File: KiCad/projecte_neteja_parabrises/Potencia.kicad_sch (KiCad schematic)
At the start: 18 parts, among them K1 DIPxx-1Axx-12xD, K2 G6K-2, Q1 NPN

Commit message: SCH V1
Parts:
- HEATER: value R -> 1K
- R: renamed from R1; value R -> 4.7K
- R1: renamed from 1k; value R -> 4.7K
- R2, R3: value 10K -> 1k
- gave numbers to parts that had none: 8
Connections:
- net VDD is gone; now on net 12V: D1.1 (K), K1.13, K1.2, K1.7, K1.8, K2.1, K2.3, K2.6
- net GND: now also U2.2 (IN2), U3.2 (IN2)
- net micro: no longer R1.1
- net GATE C: now reaches R.1
- net PWM: now reaches U2.3 (IN1)
- net PWM: now also U3.3 (IN1)
- net 12V: now reaches U2.5 (VM)
- net 12V: now also U3.5 (VM)
- new net GATE B: R1.1
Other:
- note added: "BOMBAS Y CIRCUITO RELE"
- note added: "CIRCUITO RELE Y CALEFACTOR"
- note added: "DRIVERS Y MOTORES"
- note added: "FINAL DE CARRERA"
- moved on the sheet: D1, FINALCARRERA1, FINALCARRERA2, HEATER, K1, K2, M1, M2, M3, M4, Q1, R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

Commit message: UART ACABADO
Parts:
- renumbered FINALCARRERA2 to FINALCARRERA1, FINALCARRERA1 to FINALCARRERA2, HEATER to HEATER1, K2 to K1, K1 to K2, Q1 to Q2, R to R4
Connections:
- no-connect marks 2 -> 6
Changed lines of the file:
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@@
+	)
+	(no_connect
+		(at 21.59 20.32)
+	)
+	(no_connect
+		(at 41.275 34.925)
+	)
+	(no_connect
+		(at -13.97 45.72)
+	)
+	(no_connect
+		(at 41.275 65.405)
 	)
 	(no_connect
@@
 		(on_board yes)
 		(dnp no)
-		(property "Reference" "#PWR?"
+		(property "Reference" "#PWR014"
 			(at 31.115 46.355 0)
 			(effects
@@
 			(project "projecte_neteja_parabrises"
 				(path "/83fe8808-b70b-463e-9fcd-89556c9690a9/54835b05-573d-4299-97f2-a5366b1fd616"
-					(reference "#PWR?")
+					(reference "#PWR014")
 					(unit 1)
 				)
@@
 		(dnp no)
 		(fields_autoplaced yes)
-		(property "Reference" "FINALCARRERA?"
+		(property "Reference" "FINALCARRERA2"
 			(at 45.085 99.695 0)
 			(effects
@@
 			(project "projecte_neteja_parabrises"
 				(path "/83fe8808-b70b-463e-9fcd-89556c9690a9/54835b05-573d-4299-97f2-a5366b1fd616"
-					(reference "FINALCARRERA?")
+					(reference "FINALCARRERA2")
 					(unit 1)
 				)
@@
 		(dnp no)
 		(fields_autoplaced yes)
-		(property "Reference" "#PWR?"
+		(property "Reference" "#PWR021"
 			(at 254 27.305 0)
 			(effects
@@
 			(project "projecte_neteja_parabrises"
 				(path "/83fe8808-b70b-463e-9fcd-89556c9690a9/54835b05-573d-4299-97f2-a5366b1fd616"
-					(reference "#PWR?")
+					(reference "#PWR021")
 					(unit 1)
 				)
@@
 		(dnp no)
 		(fields_autoplaced yes)
-		(property "Reference" "#PWR?"
+		(property "Reference" "#PWR016"
 			(at 33.655 92.71 0)
 			(effects
@@
 			(project "projecte_neteja_parabrises"
 				(path "/83fe8808-b70b-463e-9fcd-89556c9690a9/54835b05-573d-4299-97f2-a5366b1fd616"
-					(reference "#PWR?")
+					(reference "#PWR016")
 					(unit 1)
 				)
@@
 		(dnp no)
 		(fields_autoplaced yes)
-		(property "Reference" "R"
+		(property "Reference" "R4"
 			(at 217.17 44.45 90)
 			(effects
@@
 			(project "projecte_neteja_parabrises"
 				(path "/83fe8808-b70b-463e-9fcd-89556c9690a9/54835b05-573d-4299-97f2-a5366b1fd616"
-					(reference "R")
+					(reference "R4")
 					(unit 1)
 				)
@@
 		(on_board yes)
 		(dnp no)
-		(property "Reference" "K?"
+		(property "Reference" "K2"
 			(at 220.98 36.1949 0)
 			(effects
@@
 			(project "projecte_neteja_parabrises"
 				(path "/83fe8808-b70b-463e-9fcd-89556c9690a9/54835b05-573d-4299-97f2-a5366b1fd616"
-					(reference "K?")
+					(reference "K2")
 					(unit 1)
 				)
@@
 		(dnp no)
 		(fields_autoplaced yes)
-		(property "Reference" "#PWR?"
+		(property "Reference" "#PWR017"
 			(at 35.56 130.81 0)
 			(effects
@@
 			(project "projecte_neteja_parabrises"
 				(path "/83fe8808-b70b-463e-9fcd-89556c9690a9/54835b05-573d-4299-97f2-a5366b1fd616"
-					(reference "#PWR?")
+					(reference "#PWR017")
 					(unit 1)
 				)
@@
 		(on_board yes)
 		(dnp no)
-		(property "Reference" "#PWR01"
+		(property "Reference" "#PWR0102"
 			(at 170.18 19.685 0)
 			(effects
@@
 			(project ""
 				(path "/83fe8808-b70b-463e-9fcd-89556c9690a9/54835b05-573d-4299-97f2-a5366b1fd616"
-					(reference "#PWR01")
+					(reference "#PWR0102")
 					(unit 1)
 				)
@@
 		(dnp no)
 		(fields_autoplaced yes)
-		(property "Reference" "K?"
+		(property "Reference" "K1"
 			(at 163.195 45.7199 0)
 			(effects
@@
 			(project "projecte_neteja_parabrises"
 				(path "/83fe8808-b70b-463e-9fcd-89556c9690a9/54835b05-573d-4299-97f2-a5366b1fd616"
-					(reference "K?")
+					(reference "K1")
 					(unit 1)
 				)
@@
 		(dnp no)
 		(fields_autoplaced yes)
-		(property "Reference" "R?"
+		(property "Reference" "R3"
 			(at 38.1 119.3799 0)
 			(effects
@@
 			(project "projecte_neteja_parabrises"
 				(path "/83fe8808-b70b-463e-9fcd-89556c9690a9/54835b05-573d-4299-97f2-a5366b1fd616"
-					(reference "R?")
+					(reference "R3")
 					(unit 1)
 				)
@@
 		(dnp no)
 		(fields_autoplaced yes)
-		(property "Reference" "#PWR02"
+		(property "Reference" "#PWR0103"
 			(at 174.625 27.305 0)
 			(effects
@@
 			(project ""
 				(path "/83fe8808-b70b-463e-9fcd-89556c9690a9/54835b05-573d-4299-97f2-a5366b1fd616"
-					(reference "#PWR02")
+					(reference "#PWR0103")
 					(unit 1)
 				)
@@
 		(dnp no)
 		(fields_autoplaced yes)
-		(property "Reference" "#PWR?"
+		(property "Reference" "#PWR019"
 			(at 56.515 106.68 0)
 			(effects
@@
 			(project "projecte_neteja_parabrises"
 				(path "/83fe8808-b70b-463e-9fcd-89556c9690a9/54835b05-573d-4299-97f2-a5366b1fd616"
-					(reference "#PWR?")
+					(reference "#PWR019")
 					(unit 1)
 				)
@@
 		(dnp no)
 		(fields_autoplaced yes)
-		(property "Reference" "R?"
+		(property "Reference" "R2"
 			(at 35.56 101.5999 0)
 			(effects
@@
 			(project "projecte_neteja_parabrises"
 				(path "/83fe8808-b70b-463e-9fcd-89556c9690a9/54835b05-573d-4299-97f2-a5366b1fd616"
-					(reference "R?")
+					(reference "R2")
 					(unit 1)
 				)
@@
 		(dnp no)
 		(fields_autoplaced yes)
-		(property "Reference" "HEATER"
+		(property "Reference" "HEATER1"
 			(at 243.84 21.59 90)
 			(effects
@@
 			(project "projecte_neteja_parabrises"
 				(path "/83fe8808-b70b-463e-9fcd-89556c9690a9/54835b05-573d-4299-97f2-a5366b1fd616"
-					(reference "HEATER")
+					(reference "HEATER1")
 					(unit 1)
 				)
@@
 		(dnp no)
 		(fields_autoplaced yes)
-		(property "Reference" "#PWR?"
+		(property "Reference" "#PWR020"
 			(at 228.6 61.595 0)
 			(effects
@@
 			(project "projecte_neteja_parabrises"
 				(path "/83fe8808-b70b-463e-9fcd-89556c9690a9/54835b05-573d-4299-97f2-a5366b1fd616"
-					(reference "#PWR?")
+					(reference "#PWR020")
 					(unit 1)
 				)
@@
 		(dnp no)
 		(fields_autoplaced yes)
-		(property "Reference" "#PWR?"
+		(property "Reference" "#PWR015"
 			(at 31.115 76.835 0)
 			(effects
@@
 			(project "projecte_neteja_parabrises"
 				(path "/83fe8808-b70b-463e-9fcd-89556c9690a9/54835b05-573d-4299-97f2-a5366b1fd616"
-					(reference "#PWR?")
+					(reference "#PWR015")
 					(unit 1)
 				)
@@
 		(dnp no)
 		(fields_autoplaced yes)
-		(property "Reference" "#PWR?"
+		(property "Reference" "#PWR018"
 			(at 55.88 116.84 0)
 			(effects
@@
 			(project "projecte_neteja_parabrises"
 				(path "/83fe8808-b70b-463e-9fcd-89556c9690a9/54835b05-573d-4299-97f2-a5366b1fd616"
-					(reference "#PWR?")
+					(reference "#PWR018")
 					(unit 1)
 				)
@@
 		(dnp no)
 		(fields_autoplaced yes)
-		(property "Reference" "Q?"
+		(property "Reference" "Q2"
 			(at 231.775 48.8949 0)
 			(effects
@@
 			(project "projecte_neteja_parabrises"
 				(path "/83fe8808-b70b-463e-9fcd-89556c9690a9/54835b05-573d-4299-97f2-a5366b1fd616"
-					(reference "Q?")
+					(reference "Q2")
 					(unit 1)
 				)
@@
 		(dnp no)
 		(fields_autoplaced yes)
-		(property "Reference" "FINALCARRERA?"
+		(property "Reference" "FINALCARRERA1"
 			(at 44.45 109.855 0)
 			(effects
@@
 			(project "projecte_neteja_parabrises"
 				(path "/83fe8808-b70b-463e-9fcd-89556c9690a9/54835b05-573d-4299-97f2-a5366b1fd616"
-					(reference "FINALCARRERA?")
+					(reference "FINALCARRERA1")
 					(unit 1)
 				)
@@
 		(dnp no)
 		(fields_autoplaced yes)
-		(property "Reference" "#PWR03"
+		(property "Reference" "#PWR0101"
 			(at 136.525 75.565 0)
 			(effects
@@
 			(project ""
 				(path "/83fe8808-b70b-463e-9fcd-89556c9690a9/54835b05-573d-4299-97f2-a5366b1fd616"
-					(reference "#PWR03")
-					(unit 1)
-				)
+					(reference "#PWR0101")
+					(unit 1)
+				)

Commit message: MICRO ACTUALIZADA
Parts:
- renumbered R1 to 1k, D1 to D?, FINALCARRERA2 to FINALCARRERA1, FINALCARRERA1 to FINALCARRERA2, HEATER1 to HEATER, K2 to K1, K1 to K2, M1 to M?, M3 to M?, M4 to M?, M2 to M?, Q2 to Q1, Q1 to Q?, R4 to R1, U2 to U?, U3 to U?
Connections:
- net micro: no longer FINALCARRERA1.1 (A), R2.2
- new net FC1: FINALCARRERA1.1 (A), R2.2
- no-connect marks 6 -> 5
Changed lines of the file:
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@@
-	)
-	(no_connect
-		(at 21.59 20.32)
 	)
 	(no_connect
@@
 		)
 	)
-	(global_label "micro"
+	(global_label "FC1"
 		(shape input)
 		(at 29.845 106.68 180)
@@
 		)
 		(property "Intersheetrefs" "${INTERSHEET_REFS}"
-			(at 21.5379 106.68 0)
+			(at 23.2917 106.68 0)
 			(effects
 				(font
@@
 		(on_board yes)
 		(dnp no)
-		(property "Reference" "#PWR014"
+		(property "Reference" "#PWR02"
 			(at 31.115 46.355 0)
 			(effects
@@
 		(dnp no)
 		(fields_autoplaced yes)
-		(property "Reference" "FINALCARRERA2"
+		(property "Reference" "FINALCARRERA1"
 			(at 45.085 99.695 0)
 			(effects
@@
 		(dnp no)
 		(fields_autoplaced yes)
-		(property "Reference" "#PWR021"
+		(property "Reference" "#PWR03"
 			(at 254 27.305 0)
 			(effects
@@
 		(dnp no)
 		(fields_autoplaced yes)
-		(property "Reference" "D1"
+		(property "Reference" "D?"
 			(at 128.27 45.0849 90)
 			(effects
@@
 		(dnp no)
 		(fields_autoplaced yes)
-		(property "Reference" "#PWR016"
+		(property "Reference" "#PWR08"
 			(at 33.655 92.71 0)
 			(effects
@@
 		(dnp no)
 		(fields_autoplaced yes)
-		(property "Reference" "R4"
+		(property "Reference" "R1"
 			(at 217.17 44.45 90)
 			(effects
@@
 		(on_board yes)
 		(dnp no)
-		(property "Reference" "K2"
+		(property "Reference" "K1"
 			(at 220.98 36.1949 0)
 			(effects
@@
 		(dnp no)
 		(fields_autoplaced yes)
-		(property "Reference" "U2"
+		(property "Reference" "U?"
 			(at 33.2583 17.145 0)
 			(effects
@@
 		(dnp no)
 		(fields_autoplaced yes)
-		(property "Reference" "Q1"
+		(property "Reference" "Q?"
 			(at 139.7 62.8649 0)
 			(effects
@@
 		(dnp no)
 		(fields_autoplaced yes)
-		(property "Reference" "M1"
+		(property "Reference" "M?"
 			(at 62.23 27.9399 0)
 			(effects
@@
 		(dnp no)
 		(fields_autoplaced yes)
-		(property "Reference" "#PWR017"
+		(property "Reference" "#PWR07"
 			(at 35.56 130.81 0)
 			(effects
@@
 		(on_board yes)
 		(dnp no)
-		(property "Reference" "#PWR0102"
+		(property "Reference" "#PWR?"
 			(at 170.18 19.685 0)
 			(effects
@@
 		(dnp no)
 		(fields_autoplaced yes)
-		(property "Reference" "K1"
+		(property "Reference" "K2"
 			(at 163.195 45.7199 0)
 			(effects
@@
 		(dnp no)
 		(fields_autoplaced yes)
-		(property "Reference" "#PWR0103"
+		(property "Reference" "#PWR?"
 			(at 174.625 27.305 0)
 			(effects
@@
 		(dnp no)
 		(fields_autoplaced yes)
-		(property "Reference" "#PWR019"
+		(property "Reference" "#PWR05"
 			(at 56.515 106.68 0)
 			(effects
@@
 		(dnp no)
 		(fields_autoplaced yes)
-		(property "Reference" "U3"
+		(property "Reference" "U?"
 			(at 33.2583 47.625 0)
 			(effects
@@
 		(dnp no)
 		(fields_autoplaced yes)
-		(property "Reference" "HEATER1"
+		(property "Reference" "HEATER"
 			(at 243.84 21.59 90)
 			(effects
@@
 		(on_board yes)
 		(dnp no)
-		(property "Reference" "R1"
+		(property "Reference" "1k"
 			(at 125.73 69.215 90)
 			(effects
@@
 		(dnp no)
 		(fields_autoplaced yes)
-		(property "Reference" "#PWR020"
+		(property "Reference" "#PWR04"
 			(at 228.6 61.595 0)
 			(effects
@@
 		(dnp no)
 		(fields_autoplaced yes)
-		(property "Reference" "#PWR08"
+		(property "Reference" "#PWR?"
 			(at 20.955 64.135 0)
 			(effects
@@
 		)
 		(instances
+			(project "Potencia"
+				(path "/82bf9682-9f8b-46a0-adc6-e19c50674fc0"
+					(reference "#PWR?")
+					(unit 1)
+				)
+			)
 			(project ""
 				(path "/83fe8808-b70b-463e-9fcd-89556c9690a9/54835b05-573d-4299-97f2-a5366b1fd616"
@@
 		(on_board yes)
 		(dnp no)
-		(property "Reference" "M3"
+		(property "Reference" "M?"
 			(at 164.465 24.13 90)
 			(effects
@@
 		(on_board yes)
 		(dnp no)
-		(property "Reference" "M4"
+		(property "Reference" "M?"
 			(at 155.575 24.765 90)
 			(effects
@@
 		(dnp no)
 		(fields_autoplaced yes)
-		(property "Reference" "#PWR015"
+		(property "Reference" "#PWR01"
 			(at 31.115 76.835 0)
 			(effects
@@
 		(dnp no)
 		(fields_autoplaced yes)
-		(property "Reference" "#PWR018"
+		(property "Reference" "#PWR06"
 			(at 55.88 116.84 0)
 			(effects
@@
 		(dnp no)
 		(fields_autoplaced yes)
-		(property "Reference" "Q2"
+		(property "Reference" "Q1"
 			(at 231.775 48.8949 0)
 			(effects
@@
 		(dnp no)
 		(fields_autoplaced yes)
-		(property "Reference" "FINALCARRERA1"
+		(property "Reference" "FINALCARRERA2"
 			(at 44.45 109.855 0)
 			(effects
@@
 		(dnp no)
 		(fields_autoplaced yes)
-		(property "Reference" "M2"
+		(property "Reference" "M?"
 			(at 64.77 57.7849 0)
 			(effects
@@
 		(dnp no)
 		(fields_autoplaced yes)
-		(property "Reference" "#PWR0101"
+		(property "Reference" "#PWR?"
 			(at 136.525 75.565 0)
 			(effects
@@
 		(dnp no)
 		(fields_autoplaced yes)
-		(property "Reference" "#PWR07"
+		(property "Reference" "#PWR?"
 			(at 20.955 33.655 0)
 			(effects
@@
 		)
 		(instances
+			(project "Potencia"
+				(path "/82bf9682-9f8b-46a0-adc6-e19c50674fc0"
+					(reference "#PWR?")
+					(unit 1)
+				)
+			)
 			(project ""
 				(path "/83fe8808-b70b-463e-9fcd-89556c9690a9/54835b05-573d-4299-97f2-a5366b1fd616"

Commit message: ESQUEMATICO V2
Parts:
- gave numbers to parts that had none: 8
- renumbered FINALCARRERA2 to FINALCARRERA1, FINALCARRERA1 to FINALCARRERA2, HEATER to HEATER1, K2 to K1, K1 to K2, Q1 to Q2, 1k to R1, R1 to R4
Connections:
- net PWM: no longer U3.3 (IN1)
- net micro renamed FC2
- new net PWM2: U3.3 (IN1)

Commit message: Error de nombres solucionado
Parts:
- renumbered U2 to U4
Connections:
- no-connect marks 5 -> 4
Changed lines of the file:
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@@
-	)
-	(no_connect
-		(at -13.97 45.72)
 	)
 	(no_connect
@@
 		(on_board yes)
 		(dnp no)
-		(property "Reference" "#PWR014"
+		(property "Reference" "#PWR0109"
 			(at 31.115 46.355 0)
 			(effects
@@
 			(project "projecte_neteja_parabrises"
 				(path "/83fe8808-b70b-463e-9fcd-89556c9690a9/54835b05-573d-4299-97f2-a5366b1fd616"
-					(reference "#PWR014")
+					(reference "#PWR0109")
 					(unit 1)
 				)
@@
 		(dnp no)
 		(fields_autoplaced yes)
-		(property "Reference" "U2"
-			(at 33.2583 17.145 0)
+		(property "Reference" "U4"
+			(at 33.2583 17.78 0)
 			(effects
 				(font
@@
 		)
 		(property "Value" "DRV8871DDA"
-			(at 33.2583 19.685 0)
+			(at 33.2583 20.32 0)
 			(effects
 				(font
@@
 			(project ""
 				(path "/83fe8808-b70b-463e-9fcd-89556c9690a9/54835b05-573d-4299-97f2-a5366b1fd616"
-					(reference "U2")
+					(reference "U4")
 					(unit 1)
 				)
@@
 		(dnp no)
 		(fields_autoplaced yes)
-		(property "Reference" "#PWR017"
+		(property "Reference" "#PWR0107"
 			(at 35.56 130.81 0)
 			(effects
@@
 			(project "projecte_neteja_parabrises"
 				(path "/83fe8808-b70b-463e-9fcd-89556c9690a9/54835b05-573d-4299-97f2-a5366b1fd616"
-					(reference "#PWR017")
+					(reference "#PWR0107")
 					(unit 1)
 				)
@@
 		(dnp no)
 		(fields_autoplaced yes)
-		(property "Reference" "#PWR015"
+		(property "Reference" "#PWR0108"
 			(at 31.115 76.835 0)
 			(effects
@@
 			(project "projecte_neteja_parabrises"
 				(path "/83fe8808-b70b-463e-9fcd-89556c9690a9/54835b05-573d-4299-97f2-a5366b1fd616"
-					(reference "#PWR015")
+					(reference "#PWR0108")
 					(unit 1)
 				)
@@
 		(dnp no)
 		(fields_autoplaced yes)
-		(property "Reference" "#PWR018"
+		(property "Reference" "#PWR0106"
 			(at 55.88 116.84 0)
 			(effects
@@
 			(project "projecte_neteja_parabrises"
 				(path "/83fe8808-b70b-463e-9fcd-89556c9690a9/54835b05-573d-4299-97f2-a5366b1fd616"
-					(reference "#PWR018")
-					(unit 1)
-				)
+					(reference "#PWR0106")
+					(unit 1)
+				)

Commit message: huellas
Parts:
- D1: footprint (none) -> Diode_SMD:D_0201_0603Metric_Pad0.64x0.40mm_HandSolder
- M1, M2, M3, M4: footprint (none) -> Motors:Vybronics_VZ30C1T8219732L
- R1, R2, R3, R4: footprint (none) -> Resistor_SMD:R_0603_1608Metric_Pad0.98x0.95mm_HandSolder
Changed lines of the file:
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@@
 			)
 		)
-		(property "Footprint" ""
+		(property "Footprint" "Diode_SMD:D_0201_0603Metric_Pad0.64x0.40mm_HandSolder"
 			(at 125.73 46.355 0)
 			(effects
@@
 			)
 		)
-		(property "Footprint" ""
+		(property "Footprint" "Resistor_SMD:R_0603_1608Metric_Pad0.98x0.95mm_HandSolder"
 			(at 217.17 51.943 90)
 			(effects
@@
 			)
 		)
-		(property "Footprint" ""
+		(property "Footprint" "Motors:Vybronics_VZ30C1T8219732L"
 			(at 57.785 28.956 0)
 			(effects
@@
 			)
 		)
-		(property "Footprint" ""
+		(property "Footprint" "Resistor_SMD:R_0603_1608Metric_Pad0.98x0.95mm_HandSolder"
 			(at 33.782 120.65 90)
 			(effects
@@
 			)
 		)
-		(property "Footprint" ""
+		(property "Footprint" "Resistor_SMD:R_0603_1608Metric_Pad0.98x0.95mm_HandSolder"
 			(at 31.877 102.87 90)
 			(effects
@@
 			)
 		)
-		(property "Footprint" ""
+		(property "Footprint" "Resistor_SMD:R_0603_1608Metric_Pad0.98x0.95mm_HandSolder"
 			(at 125.095 65.913 90)
 			(effects
@@
 			)
 		)
-		(property "Footprint" ""
+		(property "Footprint" "Motors:Vybronics_VZ30C1T8219732L"
 			(at 161.671 27.305 0)
 			(effects
@@
 			)
 		)
-		(property "Footprint" ""
+		(property "Footprint" "Motors:Vybronics_VZ30C1T8219732L"
 			(at 156.591 19.685 0)
 			(effects
@@
 			)
 		)
-		(property "Footprint" ""
+		(property "Footprint" "Motors:Vybronics_VZ30C1T8219732L"
 			(at 60.325 58.801 0)
 			(effects

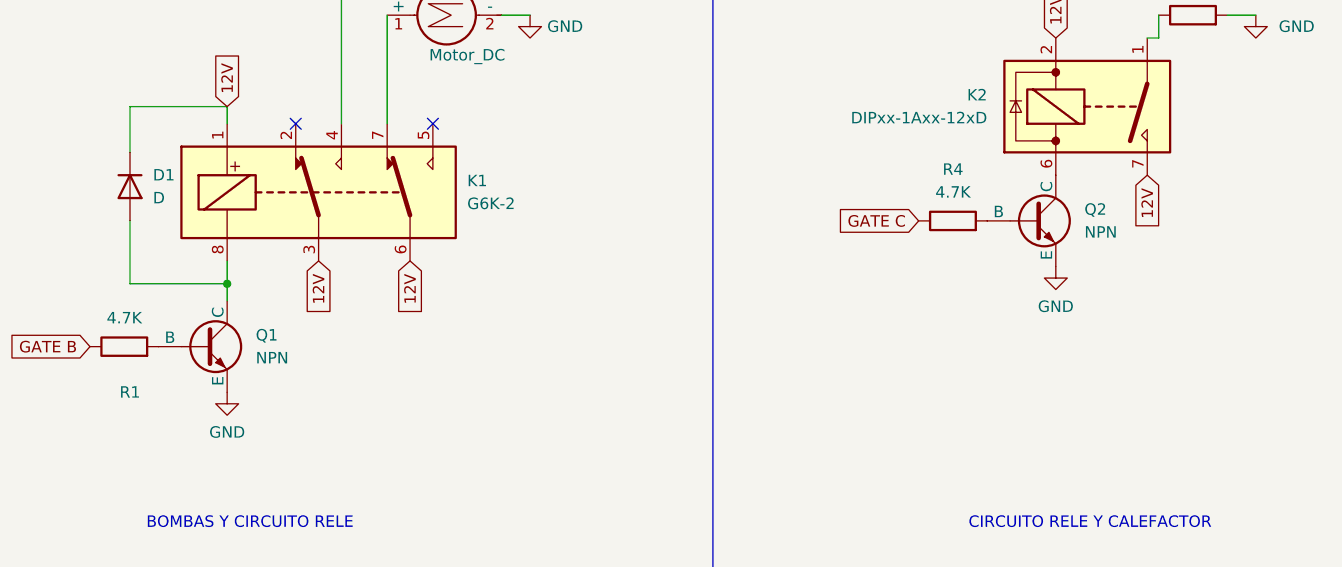
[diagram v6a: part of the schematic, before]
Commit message: Actualización huellas
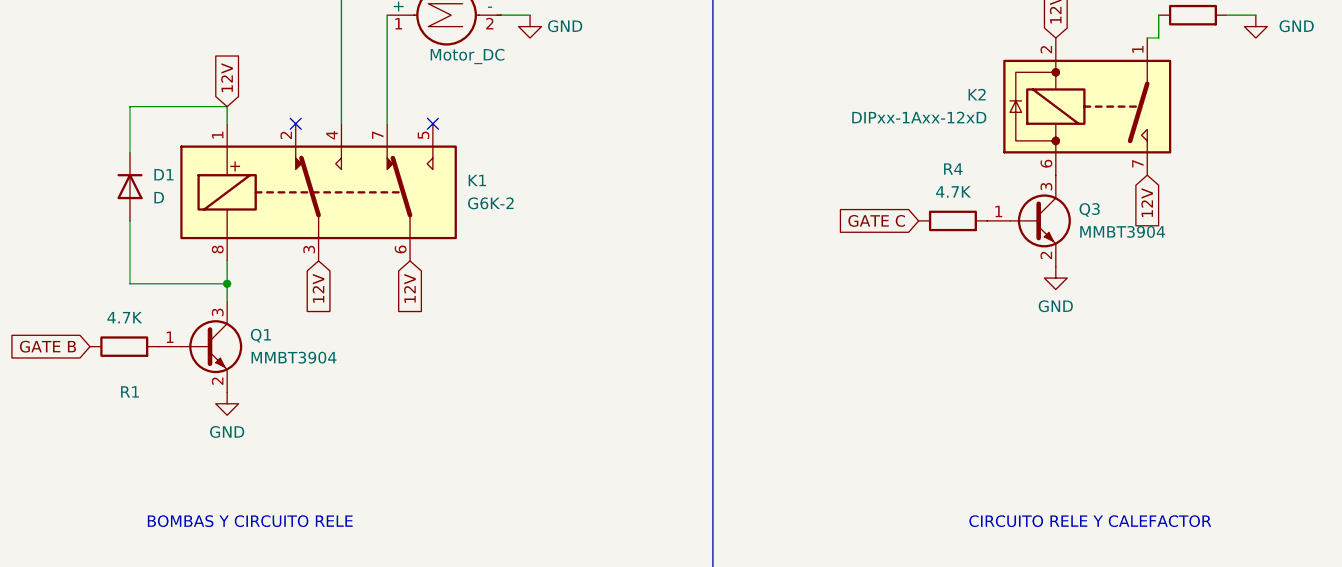
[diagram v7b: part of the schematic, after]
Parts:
- removed Q1, Q2: NPN, symbol Simulation_SPICE:NPN
- added Q1, Q3: MMBT3904, Package_TO_SOT_SMD:SOT-23, symbol Transistor_BJT:MMBT3904
- FINALCARRERA1, FINALCARRERA2: footprint (none) -> Button_Switch_THT:SW_XKB_DM1-16UC-1
- HEATER1: footprint (none) -> Resistor_SMD:R_0603_1608Metric_Pad0.98x0.95mm_HandSolder
- K1: footprint (none) -> Relay_THT:Relay_DPDT_Omron_G6K-2P
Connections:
- net GND: now also Q1.2 (E), Q3.2 (E)
- net at D1.2 (A), K1.8: now also Q1.3 (C)
- net at R4.2: now also Q3.1 (B)
- net at K2.6: now also Q3.3 (C)
- net at R1.2: now also Q1.1 (B)

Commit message: Placa definitiva
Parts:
- removed FINALCARRERA1, FINALCARRERA2: SW_SPST, Button_Switch_THT:SW_XKB_DM1-16UC-1, symbol Switch:SW_SPST
- removed K2: DIPxx-1Axx-12xD, Relay_THT:Relay_StandexMeder_DIP_LowProfile, symbol Relay:DIPxx-1Axx-12xD
- added D4: D, Diode_SMD:D_0201_0603Metric_Pad0.64x0.40mm_HandSolder, symbol Device:D
- added FINALCARRERA1, FINALCARRERA2: SW_SPDT, Button_Switch_THT:SW_XKB_DM1-16UC-1, symbol Switch:SW_SPDT
- added K3: Fujitsu_FTR-LYAA005x, Relay_THT:Relay_SPST-NO_Fujitsu_FTR-LYAA005x_FormA_Vertical, symbol Relay:Fujitsu_FTR-LYAA005x
- M1, M2, M3, M4: footprint Motors:Vybronics_VZ30C1T8219732L -> TerminalBlock:TerminalBlock_MaiXu_MX126-5.0-02P_1x02_P5.00mm
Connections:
- net 12V: now also D4.1 (K), K3.13, K3.A1
- net FC1: now also FINALCARRERA1.2 (B)
- net FC2: now also FINALCARRERA2.2 (B)
- net GND: now also FINALCARRERA1.3 (C), FINALCARRERA2.3 (C)
- net at HEATER1.1: now also K3.14
- net at Q3.3 (C): now also D4.2 (A), K3.A2
- no-connect marks 4 -> 6
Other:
- moved on the sheet: HEATER1, Q3, R2, R3, R4
